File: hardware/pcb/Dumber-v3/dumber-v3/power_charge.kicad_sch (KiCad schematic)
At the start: 42 parts, among them P1 USB_C_Plug_GCT_USB4125, Q1 PMN52XP, SW1 SW_Push, U3 LTC2954-2, U4 L6924U, U5 NCV5171, U6 TC1186

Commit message: premiers modules du firwmare dumber 3
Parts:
- removed R21: 7,5K, Resistor_SMD:R_0805_2012Metric, symbol Device:R
- added C21: 1nF, Capacitor_SMD:C_0805_2012Metric, symbol Device:C
- C10, C8: value 22µF -> 100µF; footprint Capacitor_SMD:C_0805_2012Metric -> Capacitor_SMD:C_1210_3225Metric
- C3: value 1µF -> 100µF; footprint Capacitor_SMD:C_0805_2012Metric -> Capacitor_SMD:C_1210_3225Metric
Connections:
- net +BATT: now also U4.10 (Vosns)
- net GND: now also C21.2
- net at R7.1, U4.12 (V_REF): now also C21.1
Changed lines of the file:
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@@
   (junction (at 73.66 39.37) (diameter 0) (color 0 0 0 0)
+  )
+  (junction (at 96.52 130.81) (diameter 0) (color 0 0 0 0)
   )
   (junction (at 240.03 114.3) (diameter 0) (color 0 0 0 0)
@@
     (stroke (width 0) (type default) (color 0 0 0 0))
   )
+  (wire (pts (xy 86.36 130.81) (xy 96.52 130.81))
+    (stroke (width 0) (type default) (color 0 0 0 0))
+  )
   (wire (pts (xy 29.21 175.26) (xy 36.83 175.26))
     (stroke (width 0) (type default) (color 0 0 0 0))
@@
     (stroke (width 0) (type default) (color 0 0 0 0))
   )
-  (wire (pts (xy 129.54 148.59) (xy 133.35 148.59))
+  (wire (pts (xy 119.38 148.59) (xy 133.35 148.59))
     (stroke (width 0) (type default) (color 0 0 0 0))
   )
@@
     (stroke (width 0) (type default) (color 0 0 0 0))
   )
-  (wire (pts (xy 119.38 148.59) (xy 121.92 148.59))
-    (stroke (width 0) (type default) (color 0 0 0 0))
-  )
   (polyline (pts (xy 138.43 34.29) (xy 153.67 34.29))
     (stroke (width 0) (type default) (color 0 0 0 0))
@@
   )
   (wire (pts (xy 36.83 77.47) (xy 29.21 77.47))
+    (stroke (width 0) (type default) (color 0 0 0 0))
+  )
+  (wire (pts (xy 86.36 138.43) (xy 86.36 139.7))
     (stroke (width 0) (type default) (color 0 0 0 0))
   )
@@
     )
     (property "Datasheet" "~" (id 3) (at 171.45 152.146 90)
-      (effects (font (size 1.27 1.27)) hide)
-    )
-    (pin "1")
-    (pin "2")
-  )
-  (symbol (lib_id "Device:R") (at 125.73 148.59 90) (unit 1)
-    (in_bom yes) (on_board yes) (fields_autoplaced)
-    (property "Reference" "R21" (id 0) (at 125.73 143.8742 90))
-    (property "Value" "7,5K" (id 1) (at 125.73 146.4111 90))
-    (property "Footprint" "Resistor_SMD:R_0805_2012Metric" (id 2) (at 125.73 150.368 90)
-      (effects (font (size 1.27 1.27)) hide)
-    )
-    (property "Datasheet" "~" (id 3) (at 125.73 148.59 0)
       (effects (font (size 1.27 1.27)) hide)
     )
@@
       (effects (font (size 1.27 1.27)) (justify left))
     )
-    (property "Value" "1µF" (id 1) (at 67.691 151.5622 0)
-      (effects (font (size 1.27 1.27)) (justify left))
-    )
-    (property "Footprint" "Capacitor_SMD:C_0805_2012Metric" (id 2) (at 65.7352 153.67 0)
+    (property "Value" "100µF" (id 1) (at 67.691 151.5622 0)
+      (effects (font (size 1.27 1.27)) (justify left))
+    )
+    (property "Footprint" "Capacitor_SMD:C_1210_3225Metric" (id 2) (at 65.7352 153.67 0)
       (effects (font (size 1.27 1.27)) hide)
     )
@@
     (pin "1")
     (pin "2")
+  )
+  (symbol (lib_id "power:GND") (at 86.36 139.7 0) (unit 1)
+    (in_bom yes) (on_board yes) (fields_autoplaced)
+    (property "Reference" "#PWR01" (id 0) (at 86.36 146.05 0)
+      (effects (font (size 1.27 1.27)) hide)
+    )
+    (property "Value" "GND" (id 1) (at 86.36 144.1434 0))
+    (property "Footprint" "" (id 2) (at 86.36 139.7 0)
+      (effects (font (size 1.27 1.27)) hide)
+    )
+    (property "Datasheet" "" (id 3) (at 86.36 139.7 0)
+      (effects (font (size 1.27 1.27)) hide)
+    )
+    (pin "1")
   )
   (symbol (lib_id "Device:C") (at 120.65 87.63 0) (unit 1)
@@
     (pin "1")
   )
+  (symbol (lib_id "Device:C") (at 86.36 134.62 0) (unit 1)
+    (in_bom yes) (on_board yes) (fields_autoplaced)
+    (property "Reference" "C21" (id 0) (at 89.281 133.7853 0)
+      (effects (font (size 1.27 1.27)) (justify left))
+    )
+    (property "Value" "1nF" (id 1) (at 89.281 136.3222 0)
+      (effects (font (size 1.27 1.27)) (justify left))
+    )
+    (property "Footprint" "Capacitor_SMD:C_0805_2012Metric" (id 2) (at 87.3252 138.43 0)
+      (effects (font (size 1.27 1.27)) hide)
+    )
+    (property "Datasheet" "~" (id 3) (at 86.36 134.62 0)
+      (effects (font (size 1.27 1.27)) hide)
+    )
+    (pin "1")
+    (pin "2")
+  )
   (symbol (lib_id "power:GND") (at 146.05 59.69 0) (unit 1)
     (in_bom yes) (on_board yes) (fields_autoplaced)
@@
       (effects (font (size 1.27 1.27)) (justify left))
     )
-    (property "Value" "22µF" (id 1) (at 187.071 105.8422 0)
-      (effects (font (size 1.27 1.27)) (justify left))
-    )
-    (property "Footprint" "Capacitor_SMD:C_0805_2012Metric" (id 2) (at 185.1152 107.95 0)
+    (property "Value" "100µF" (id 1) (at 187.071 105.8422 0)
+      (effects (font (size 1.27 1.27)) (justify left))
+    )
+    (property "Footprint" "Capacitor_SMD:C_1210_3225Metric" (id 2) (at 185.1152 107.95 0)
       (effects (font (size 1.27 1.27)) hide)
     )
@@
       (effects (font (size 1.27 1.27)) (justify left))
     )
-    (property "Value" "22µF" (id 1) (at 164.211 105.8422 0)
-      (effects (font (size 1.27 1.27)) (justify left))
-    )
-    (property "Footprint" "Capacitor_SMD:C_0805_2012Metric" (id 2) (at 162.2552 107.95 0)
-      (effects (font (size 1.27 1.27)) hide)
-    )
+    (property "Value" "100µF" (id 1) (at 164.211 105.8422 0)
+      (effects (font (size 1.27 1.27)) (justify left))
+    )
+    (property "Footprint" "Capacitor_SMD:C_1210_3225Metric" (id 2) (at 162.2552 107.95 0)
+      (effects (font (size 1.27 1.27)) hide)
+    )

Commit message: Mise a jour PCB et coque. Des fichiers STEP ne sont pas encore remontés car trop gros
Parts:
- removed L2: 22µH, Inductor_SMD:L_Taiyo-Yuden_MD-4040, symbol Device:L
- removed U3: LTC2954-2, Package_TO_SOT_SMD:SOT-23-8, symbol Insa:LTC2954
- removed U5: NCV5171, Package_SO:SO-8_3.9x4.9mm_P1.27mm, symbol Insa:NCV5171
- added H1, H2, H3: MountingHole, MountingHole:MountingHole_3.2mm_M3_ISO14580, symbol Mechanical:MountingHole
- added L1: 10µH, Inductor_SMD:L_Bourns_SRP7028A_7.3x6.6mm, symbol Device:L
- added U3: LTC2954-2, Package_TO_SOT_SMD:SOT-23-8, symbol Insa:LTC2954-2
- added U5: LM2731XMF, Package_TO_SOT_SMD:SOT-23-5, symbol Regulator_Switching:LM2731XMF
- C10: value 100µF -> 10µF
- C5: value 100nF -> 2.2µF
- C8: value 100µF -> 650pF; footprint Capacitor_SMD:C_1210_3225Metric -> Capacitor_SMD:C_0805_2012Metric
- R10: value 3.72K -> 40.2K
- R11: value 1.28K -> 13.3K
- R8: value 5K -> 47K
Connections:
- net +5V: now also C8.2, R10.1; no longer R10.2
- net +BATT: now also U3.1 (Vin)
- net BUTTON_SENSE: now also U3.5 (~{INT})
- net GND: now also C5.2, U3.4 (GND), U5.2 (GND); no longer C8.2, R8.1
- net SHUTDOWN: now also U3.8 (~{KILL})
- net SHUTDOWN_5V: now also R8.1, U5.4 (EN)
- net at C5.1: now also C6.1, D1.3 (A), R15.2, R8.2, U6.1 (Vin), U6.3 (~{SHDN}), L1.1, U5.5 (VIN)
- net BUTTON_PRESS: now reaches SW1.2
- net BUTTON_PRESS: now also U3.2 (~{PB})
- net at D2.2 (A): now also L1.2, U5.1 (SW)
- net at C1.1: now also U3.3 (ONT)
- net at R1.1, R2.2: now also U3.6 (~{EN})
- net at C2.1: now also U3.7 (PDT)
- net at R11.2: now also C8.1, R10.2, U5.3 (FB); no longer R10.1
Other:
- moved on the sheet: C10, C5, D2, R10, R11, R8

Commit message: Mise a jour sur les pcbs de dumber v3
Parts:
- removed R15: 1M, Resistor_SMD:R_0805_2012Metric, symbol Device:R
- R12, R14: value 25.5K -> 15K
- R13: value 2.2K -> 300
- R9: value 470R -> 470
- U6: value TC1186 -> AP2206
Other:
- note added: "Do not populate"
- note removed: "Populate only if AP2202K-2.6TRE is used"
- note removed: "Populate only if TC1186 is used"
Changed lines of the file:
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@@
   (junction (at 152.4 85.09) (diameter 0) (color 0 0 0 0)
-  )
-  (junction (at 161.29 44.45) (diameter 0) (color 0 0 0 0)
   )
   (junction (at 171.45 156.21) (diameter 0) (color 0 0 0 0)
@@
     (stroke (width 0) (type default) (color 0 0 0 0))
   )
+  (polyline (pts (xy 149.86 165.1) (xy 160.02 165.1))
+    (stroke (width 0) (type default) (color 0 0 0 0))
+  )
+  (polyline (pts (xy 160.02 175.26) (xy 149.86 175.26))
+    (stroke (width 0) (type default) (color 0 0 0 0))
+  )
   (wire (pts (xy 129.54 85.09) (xy 129.54 95.25))
     (stroke (width 0) (type default) (color 0 0 0 0))
   )
-  (polyline (pts (xy 153.67 34.29) (xy 153.67 19.05))
-    (stroke (width 0) (type default) (color 0 0 0 0))
-  )
   (wire (pts (xy 86.36 130.81) (xy 96.52 130.81))
     (stroke (width 0) (type default) (color 0 0 0 0))
@@
     (stroke (width 0) (type default) (color 0 0 0 0))
   )
+  (polyline (pts (xy 149.86 165.1) (xy 149.86 175.26))
+    (stroke (width 0) (type default) (color 0 0 0 0))
+  )
   (wire (pts (xy 29.21 63.5) (xy 29.21 44.45))
     (stroke (width 0) (type default) (color 0 0 0 0))
@@
     (stroke (width 0) (type default) (color 0 0 0 0))
   )
+  (polyline (pts (xy 160.02 175.26) (xy 160.02 179.07))
+    (stroke (width 0) (type default) (color 0 0 0 0))
+  )
   (wire (pts (xy 77.47 190.5) (xy 86.36 190.5))
     (stroke (width 0) (type default) (color 0 0 0 0))
@@
     (stroke (width 0) (type default) (color 0 0 0 0))
   )
-  (wire (pts (xy 133.35 41.91) (xy 133.35 29.21))
-    (stroke (width 0) (type default) (color 0 0 0 0))
-  )
   (wire (pts (xy 154.94 90.17) (xy 161.29 90.17))
     (stroke (width 0) (type default) (color 0 0 0 0))
@@
     (stroke (width 0) (type default) (color 0 0 0 0))
   )
-  (polyline (pts (xy 138.43 19.05) (xy 153.67 19.05))
-    (stroke (width 0) (type default) (color 0 0 0 0))
-  )
   (wire (pts (xy 152.4 85.09) (xy 161.29 85.09))
     (stroke (width 0) (type default) (color 0 0 0 0))
   )
-  (polyline (pts (xy 177.8 54.61) (xy 177.8 60.96))
-    (stroke (width 0) (type default) (color 0 0 0 0))
-  )
   (wire (pts (xy 76.2 71.12) (xy 90.17 71.12))
     (stroke (width 0) (type default) (color 0 0 0 0))
@@
     (stroke (width 0) (type default) (color 0 0 0 0))
   )
-  (wire (pts (xy 161.29 29.21) (xy 161.29 44.45))
-    (stroke (width 0) (type default) (color 0 0 0 0))
-  )
   (wire (pts (xy 137.16 90.17) (xy 137.16 92.71))
     (stroke (width 0) (type default) (color 0 0 0 0))
@@
     (stroke (width 0) (type default) (color 0 0 0 0))
   )
-  (polyline (pts (xy 170.18 45.72) (xy 170.18 54.61))
-    (stroke (width 0) (type default) (color 0 0 0 0))
-  )
-  (polyline (pts (xy 170.18 54.61) (xy 156.21 54.61))
-    (stroke (width 0) (type default) (color 0 0 0 0))
-  )
   (wire (pts (xy 19.05 71.12) (xy 36.83 71.12))
     (stroke (width 0) (type default) (color 0 0 0 0))
@@
     (stroke (width 0) (type default) (color 0 0 0 0))
   )
-  (polyline (pts (xy 170.18 54.61) (xy 177.8 54.61))
-    (stroke (width 0) (type default) (color 0 0 0 0))
-  )
   (wire (pts (xy 119.38 156.21) (xy 142.24 156.21))
     (stroke (width 0) (type default) (color 0 0 0 0))
@@
     (stroke (width 0) (type default) (color 0 0 0 0))
   )
-  (polyline (pts (xy 138.43 34.29) (xy 153.67 34.29))
-    (stroke (width 0) (type default) (color 0 0 0 0))
-  )
   (wire (pts (xy 19.05 90.17) (xy 19.05 88.9))
     (stroke (width 0) (type default) (color 0 0 0 0))
@@
     (stroke (width 0) (type default) (color 0 0 0 0))
   )
-  (polyline (pts (xy 156.21 45.72) (xy 170.18 45.72))
-    (stroke (width 0) (type default) (color 0 0 0 0))
-  )
   (wire (pts (xy 127 41.91) (xy 133.35 41.91))
     (stroke (width 0) (type default) (color 0 0 0 0))
@@
     (stroke (width 0) (type default) (color 0 0 0 0))
   )
-  (polyline (pts (xy 138.43 19.05) (xy 138.43 34.29))
-    (stroke (width 0) (type default) (color 0 0 0 0))
-  )
   (wire (pts (xy 96.52 165.1) (xy 90.17 165.1))
     (stroke (width 0) (type default) (color 0 0 0 0))
@@
     (stroke (width 0) (type default) (color 0 0 0 0))
   )
-  (wire (pts (xy 149.86 29.21) (xy 161.29 29.21))
-    (stroke (width 0) (type default) (color 0 0 0 0))
-  )
   (wire (pts (xy 62.23 77.47) (xy 62.23 81.28))
     (stroke (width 0) (type default) (color 0 0 0 0))
@@
     (stroke (width 0) (type default) (color 0 0 0 0))
   )
-  (polyline (pts (xy 156.21 45.72) (xy 156.21 54.61))
-    (stroke (width 0) (type default) (color 0 0 0 0))
-  )
-  (wire (pts (xy 133.35 29.21) (xy 142.24 29.21))
-    (stroke (width 0) (type default) (color 0 0 0 0))
-  )
   (wire (pts (xy 240.03 110.49) (xy 240.03 114.3))
     (stroke (width 0) (type default) (color 0 0 0 0))
@@
     (stroke (width 0) (type default) (color 0 0 0 0))
   )
+  (polyline (pts (xy 160.02 165.1) (xy 160.02 175.26))
+    (stroke (width 0) (type default) (color 0 0 0 0))
+  )
   (wire (pts (xy 105.41 172.72) (xy 109.22 172.72))
     (stroke (width 0) (type default) (color 0 0 0 0))
@@
     (stroke (width 0) (type default) (color 0 0 0 0))
   )
-  (text "Populate only \nif AP2202K-2.6TRE\nis used\n" (at 179.07 60.96 0)
-    (effects (font (size 1.27 1.27)) (justify left bottom))
-  )
-  (text "Populate only \nif TC1186 is used" (at 154.94 22.86 0)
+  (text "Do not populate\n" (at 152.4 181.61 0)
     (effects (font (size 1.27 1.27)) (justify left bottom))
   )
@@
     (in_bom yes) (on_board yes) (fields_autoplaced)
     (property "Reference" "R9" (id 0) (at 125.73 126.0942 90))
-    (property "Value" "470R" (id 1) (at 125.73 128.6311 90))
+    (property "Value" "470" (id 1) (at 125.73 128.6311 90))
     (property "Footprint" "Resistor_SMD:R_0805_2012Metric" (id 2) (at 125.73 132.588 90)
       (effects (font (size 1.27 1.27)) hide)
@@
       (effects (font (size 1.27 1.27)) (justify left))
     )
-    (property "Value" "2.2K" (id 1) (at 144.018 170.6122 0)
+    (property "Value" "300" (id 1) (at 144.018 170.6122 0)
       (effects (font (size 1.27 1.27)) (justify left))
     )
@@
       (effects (font (size 1.27 1.27)) (justify left))
     )
-    (property "Value" "25.5K" (id 1) (at 132.588 170.6122 0)
+    (property "Value" "15K" (id 1) (at 132.588 170.6122 0)
       (effects (font (size 1.27 1.27)) (justify left))
     )
@@
       (effects (font (size 1.27 1.27)) (justify left))
     )
-    (property "Value" "25.5K" (id 1) (at 154.178 170.6122 0)
+    (property "Value" "15K" (id 1) (at 154.178 170.6122 0)
       (effects (font (size 1.27 1.27)) (justify left))
     )
@@
     (pin "2")
   )
-  (symbol (lib_id "Device:R") (at 146.05 29.21 270) (unit 1)
-    (in_bom yes) (on_board yes) (fields_autoplaced)
-    (property "Reference" "R15" (id 0) (at 146.05 24.4942 90))
-    (property "Value" "1M" (id 1) (at 146.05 27.0311 90))
-    (property "Footprint" "Resistor_SMD:R_0805_2012Metric" (id 2) (at 146.05 27.432 90)
-      (effects (font (size 1.27 1.27)) hide)
-    )
-    (property "Datasheet" "~" (id 3) (at 146.05 29.21 0)
-      (effects (font (size 1.27 1.27)) hide)
-    )
-    (pin "1")
-    (pin "2")
-  )
   (symbol (lib_id "power:VBUS") (at 64.77 134.62 0) (unit 1)
     (in_bom yes) (on_board yes) (fields_autoplaced)
@@
     (in_bom yes) (on_board yes) (fields_autoplaced)
     (property "Reference" "U6" (id 0) (at 146.05 36.9402 0))
-    (property "Value" "TC1186" (id 1) (at 146.05 39.4771 0))
+    (property "Value" "AP2206" (id 1) (at 146.05 39.4771 0))
     (property "Footprint" "Package_TO_SOT_SMD:SOT-23-5" (id 2) (at 146.05 37.465 0)
       (effects (font (size 1.27 1.27)) hide)

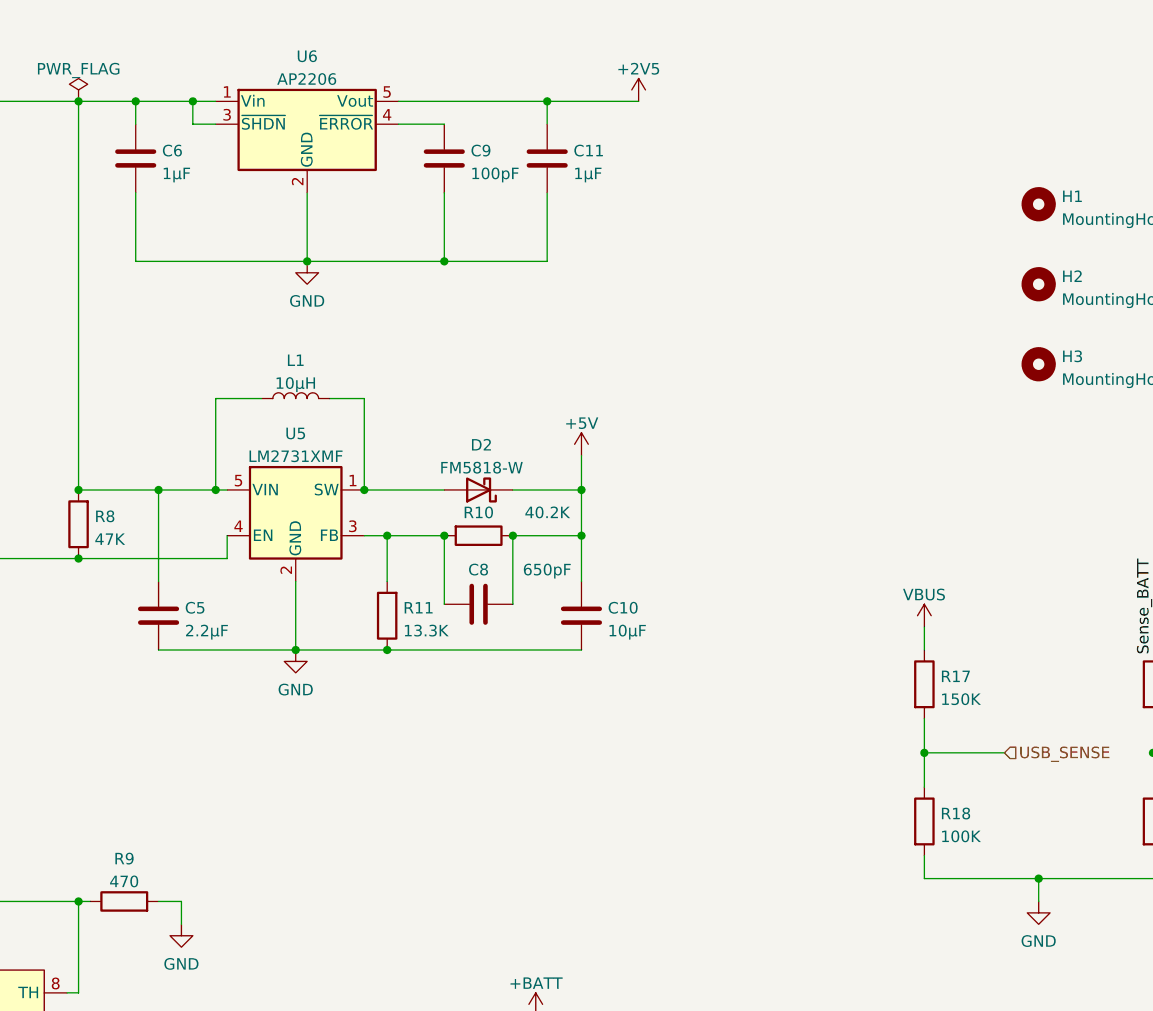
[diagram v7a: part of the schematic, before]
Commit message: PCB V2.2 avec une self sur AVDD
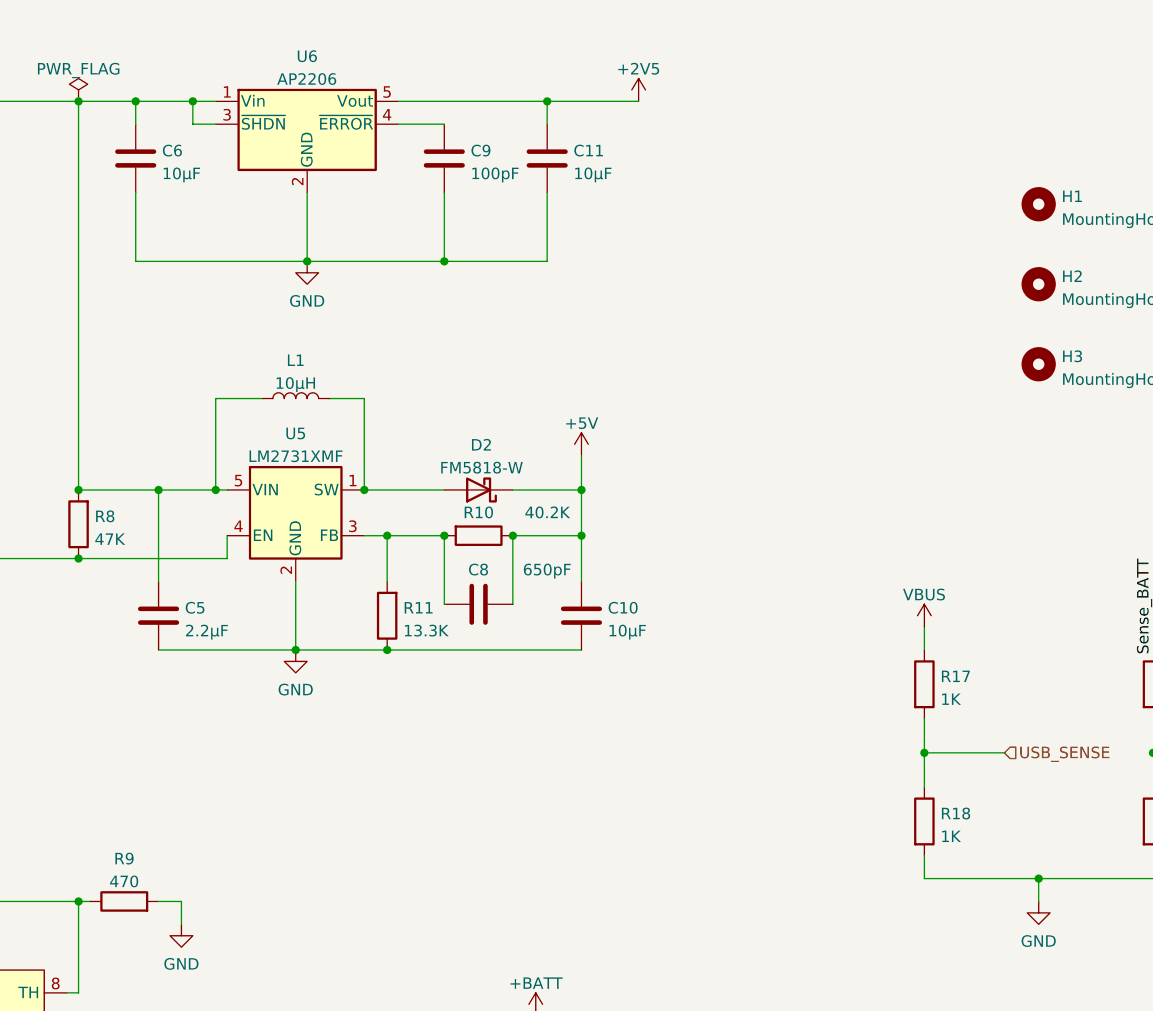
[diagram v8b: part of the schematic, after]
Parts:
- C11, C6: value 1µF -> 10µF
- R17: value 150K -> 1K
- R18: value 100K -> 1K
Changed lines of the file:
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@@
   (title_block
     (title "Power & Charge")
-    (date "2022-06-08")
-    (rev "2.0")
+    (date "2023-04-14")
+    (rev "2.1")
     (company "INSA - GEI")
   )
@@
       (effects (font (size 1.27 1.27)) (justify left))
     )
-    (property "Value" "150K" (id 1) (at 216.408 108.3822 0)
+    (property "Value" "1K" (id 1) (at 216.408 108.3822 0)
       (effects (font (size 1.27 1.27)) (justify left))
     )
@@
       (effects (font (size 1.27 1.27)) (justify left))
     )
-    (property "Value" "1µF" (id 1) (at 175.641 49.9622 0)
+    (property "Value" "10µF" (id 1) (at 175.641 49.9622 0)
       (effects (font (size 1.27 1.27)) (justify left))
     )
@@
       (effects (font (size 1.27 1.27)) (justify left))
     )
-    (property "Value" "1µF" (id 1) (at 129.921 49.9622 0)
+    (property "Value" "10µF" (id 1) (at 129.921 49.9622 0)
       (effects (font (size 1.27 1.27)) (justify left))
     )
@@
       (effects (font (size 1.27 1.27)) (justify left))
     )
-    (property "Value" "100K" (id 1) (at 216.408 123.6222 0)
-      (effects (font (size 1.27 1.27)) (justify left))
-    )
+    (property "Value" "1K" (id 1) (at 216.408 123.6222 0)
+      (effects (font (size 1.27 1.27)) (justify left))
+    )
